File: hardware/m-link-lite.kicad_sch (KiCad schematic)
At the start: 22 parts, among them J1 BEC IN, J2 PROGRAM, J3 SIG, U1 AP1117-50, U2 MCP1702-3v3, U3 74LS365, U4 ESP-12F

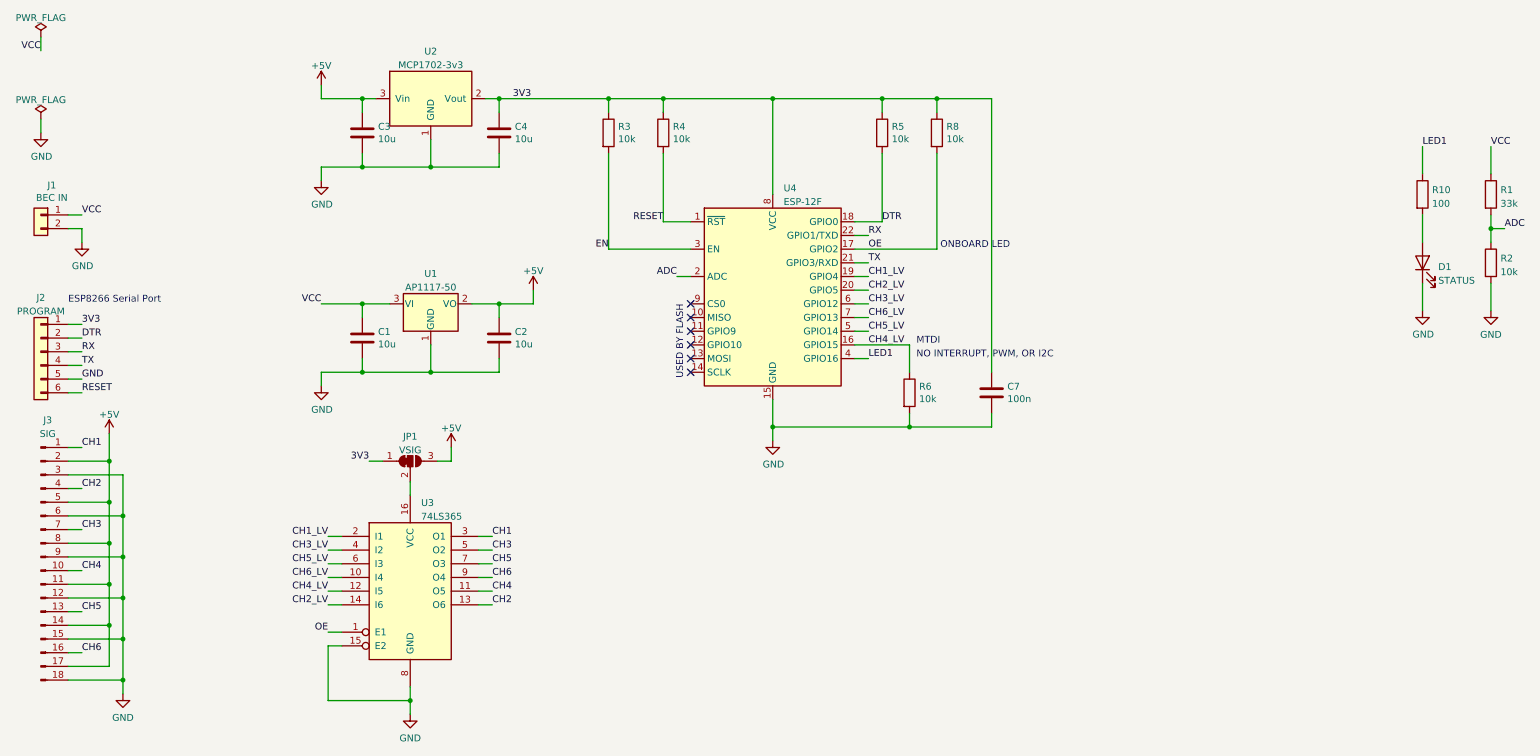
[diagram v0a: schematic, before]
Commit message: Power supply rework.
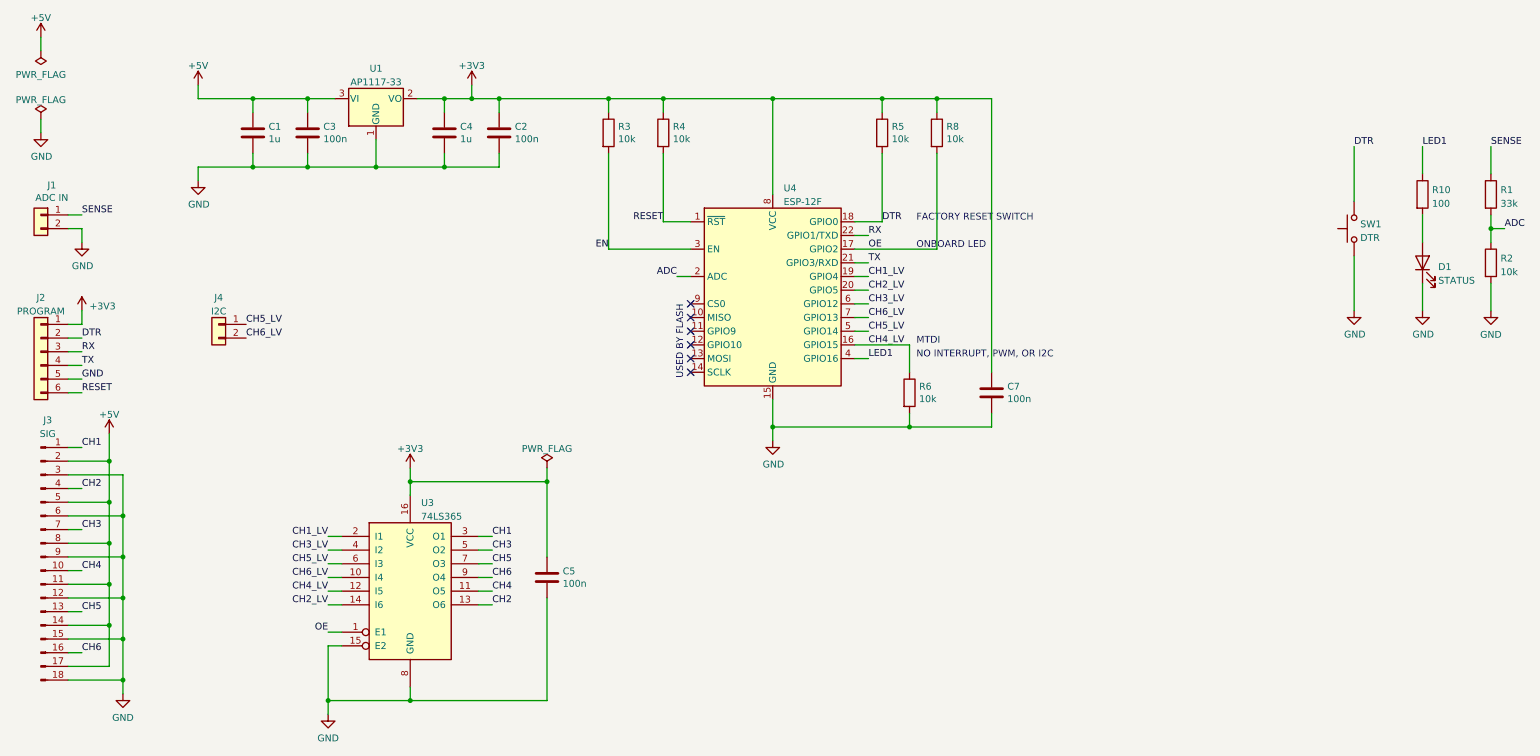
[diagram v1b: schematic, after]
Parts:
- removed JP1: VSIG, Jumper:SolderJumper-3_P1.3mm_Bridged2Bar12_RoundedPad1.0x1.5mm, symbol Jumper:SolderJumper_3_Bridged12
- removed U1: AP1117-50, Package_TO_SOT_SMD:SOT-223-3_TabPin2, symbol Regulator_Linear:AP1117-50
- removed U2: MCP1702-3v3, Package_TO_SOT_SMD:SOT-23, symbol moop-items:MCP1702-3v3
- added C5: 100n, Capacitor_SMD:C_0603_1608Metric, symbol Device:C
- added J4: I2C, symbol Connector_Generic:Conn_01x02
- added SW1: DTR, new_moop_items:SW_SPST_PTS810, symbol Switch:SW_Push
- added U1: AP1117-33, Package_TO_SOT_SMD:SOT-223-3_TabPin2, symbol Regulator_Linear:AP1117-33
- C1, C4: value 10u -> 1u
- C2, C3: value 10u -> 100n
- J1: value BEC IN -> ADC IN
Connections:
- net 3V3 is gone; now on net +3V3: C4.1, C7.1, J2.1 (Pin_1), R3.1, R4.1, R5.1, R8.1, U4.8 (VCC)
- net +5V: now also C1.1, U1.3 (VI); no longer C2.1
- net CH5_LV: now also J4.1 (Pin_1)
- net CH6_LV: now also J4.2 (Pin_2)
- net DTR: now also SW1.2
- net GND: now also C5.2, SW1.1, U1.1 (GND)
- net +3V3: now reaches U3.16 (VCC)
- net +3V3: now also C2.1, C5.1, U1.2 (VO)
- net VCC renamed SENSE
- net SENSE: no longer C1.1
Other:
- note added: "FACTORY RESET SWITCH"
- note removed: "ESP8266 Serial Port"
- moved on the sheet: C1, C2, C3, C4

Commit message: Rework v1.2 layout.
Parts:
- SW1: value DTR -> RESTORE SETTINGS
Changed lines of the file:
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@@
       (effects (font (size 1.27 1.27)) (justify right))
     )
-    (property "Value" "DTR" (id 1) (at 267.843 62.6622 90)
+    (property "Value" "RESTORE SETTINGS" (id 1) (at 267.843 62.6622 90)
       (effects (font (size 1.27 1.27)) (justify right))
     )
@@
     )
     (path "/c91f3a05-92b7-4af6-9fa5-e9872bd4952c"
-      (reference "SW1") (unit 1) (value "DTR") (footprint "new_moop_items:SW_SPST_PTS810")
+      (reference "SW1") (unit 1) (value "RESTORE SETTINGS") (footprint "new_moop_items:SW_SPST_PTS810")
     )
     (path "/67b22c72-045a-4f97-be2d-4eb7aa530e09"
